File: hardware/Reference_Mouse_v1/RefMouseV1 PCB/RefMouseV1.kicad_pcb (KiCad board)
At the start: 2 copper layers, 14 parts, among them M1 BATTBALANCE-2S, U1 TPS6205X, U2 STM32F103RX

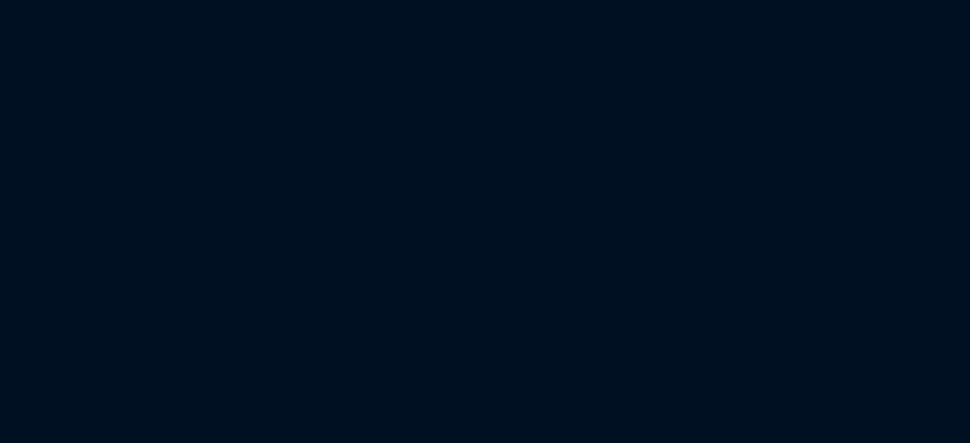
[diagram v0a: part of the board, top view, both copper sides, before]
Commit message: Added DRV sch symbol and motor sub-schematic.
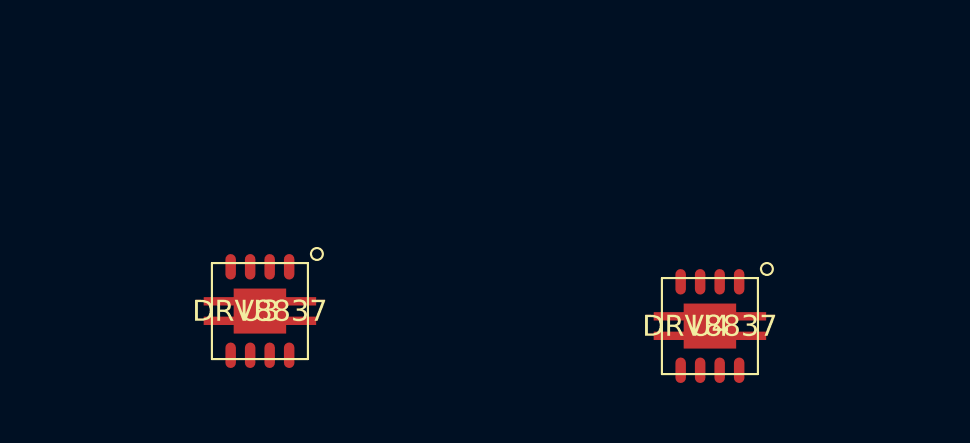
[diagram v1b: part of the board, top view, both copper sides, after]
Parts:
- added U3: DRV8837, S-PWSON-N8, F.Cu at (57.5, 71.0)
- added U4: DRV8837, S-PWSON-N8, F.Cu at (72.5, 71.5)
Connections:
- net /RefMouseV1-Power/+3.3V renamed /Power/+3.3V
- net /RefMouseV1-Power/SW renamed /Power/SW
- net /RefMouseV1-Power/VBATT renamed /Power/VBATT
- net /RefMouseV1-Power/VBATT_SW renamed /Power/VBATT_SW
